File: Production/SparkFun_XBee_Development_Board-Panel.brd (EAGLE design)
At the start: 105.7 x 224.8 mm, 822 parts, among them J1 USB Female Type C Connector, J13 QWIIC_RIGHT_ANGLE, J14 USB Female Type C Connector, J17 USB Female Type C Connector, J23 QWIIC_RIGHT_ANGLE, J24 USB Female Type C Connector, J27 USB Female Type C Connector, J3 USB Female Type C Connector, J33 QWIIC_RIGHT_ANGLE, J34 USB Female Type C Connector, J37 USB Female Type C Connector, J4 QWIIC_RIGHT_ANGLE, J43 QWIIC_RIGHT_ANGLE, J44 USB Female Type C Connector, J47 USB Female Type C Connector, J53 QWIIC_RIGHT_ANGLE, J54 USB Female Type C Connector, J57 USB Female Type C Connector, Q1 3.1A/30V/105mΩ, Q2 3.1A/30V/105mΩ, Q3 3.1A/30V/105mΩ, Q4 3.1A/30V/105mΩ, Q5 3.1A/30V/105mΩ, Q6 3.1A/30V/105mΩ, U1 FSUSB30MUX_MSOP10, U10 FT231XS, U11 FSUSB30MUX_MSOP10, U12 AP63203, U13 ESD Diode, U14 ESD Diode, U15 FT231XS, U16 FSUSB30MUX_MSOP10, U17 AP63203, U18 ESD Diode, U19 ESD Diode, U2 AP63203, U20 FT231XS, U21 FSUSB30MUX_MSOP10, U22 AP63203, U23 ESD Diode, U24 ESD Diode, U25 FT231XS, U26 FSUSB30MUX_MSOP10, U27 AP63203, U28 ESD Diode, U29 ESD Diode, U3 ESD Diode, U30 FT231XS, U4 FSUSB30MUX_MSOP10, U5 ESD Diode, U6 AP63203, U7 FT231XS, U8 ESD Diode, U9 ESD Diode

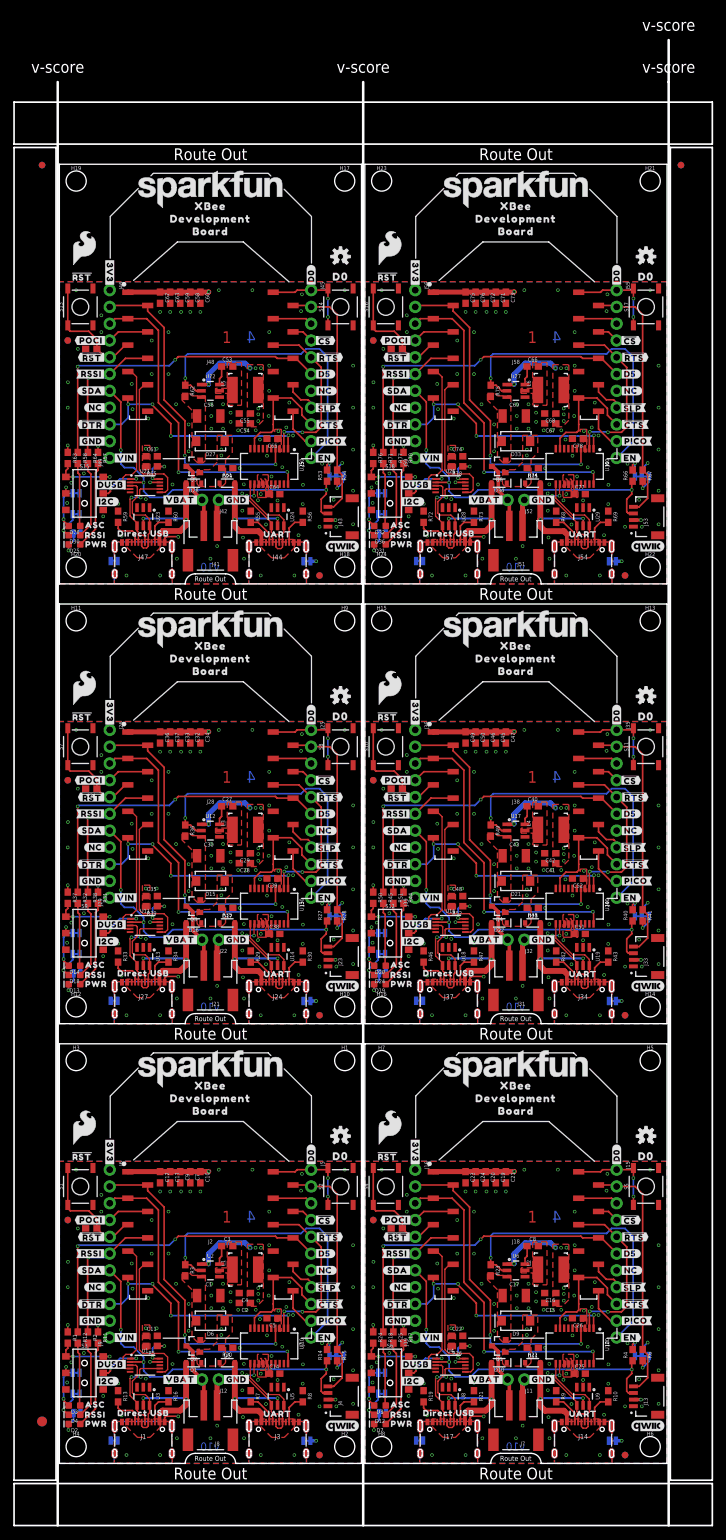
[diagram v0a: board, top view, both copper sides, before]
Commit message: Panelizes new board design
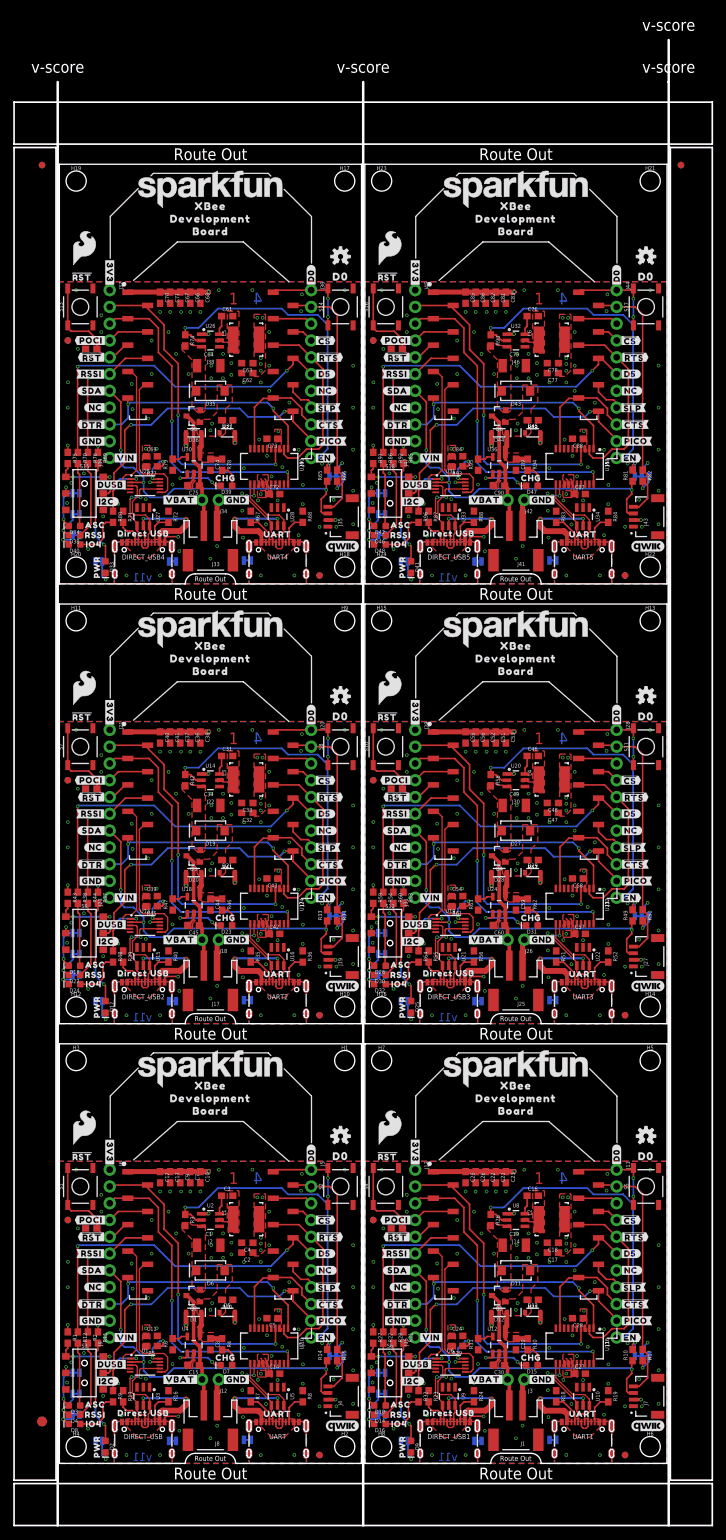
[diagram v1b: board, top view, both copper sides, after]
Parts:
- removed J49, J50, J59, J60: (no value), SparkFun-Connectors:1X01_NO_SILK_STAND
- removed J51: (no value), SparkFun-Connectors:JST-2-SMD
- removed J52: (no value), SparkFun-Connectors:1X02_NO_SILK
- removed J53: QWIIC_RIGHT_ANGLE, SparkFun-Connectors:JST04_1MM_RA
- removed J55, J56: (no value), SparkFun-Connectors:1X10_NO_SILK
- removed J58: (no value), xbee_smart_modem:XBEE3-SMD
- added C79: 10uF, SparkFun-Capacitors:1210
- added C80, C81: 10nF, SparkFun-Capacitors:0603
- added C82, C84, C87, C88: 0.1uF, SparkFun-Capacitors:0603
- added C83: 10uF, SparkFun-Capacitors:0603
- added C85: 10pF, SparkFun-Capacitors:0603
- added C86: 47pF, SparkFun-Capacitors:0603
- added C89, C90: 4.7uF, SparkFun-Capacitors:0603
- added D37, D44, D45: 3A/10V/280mV, SparkFun-DiscreteSemi:SOD-323
- added D38, D39, D46, D47: Yellow, SparkFun-LED:LED-0603
- added D40, D48: GREEN, SparkFun-LED:LED-0603
- added D41: RED, SparkFun-LED:LED-0603
- added D42: BLUE, SparkFun-LED:LED-0603
- added D43: 3A/40V/500mV, SparkFun-DiscreteSemi:SMA-DIODE
- added DIRECT_USB, DIRECT_USB1, DIRECT_USB2, DIRECT_USB3, DIRECT_USB4, UART, UART1, UART2, UART3, UART4: USB Female Type C Connector, SparkFun-Connectors:USB-C-16P-4LAYER-ISOLATED
- added IOLED, IOLED1, IOLED2, IOLED3, IOLED4, IOLED5: JUMPER-SMT_2_NC_TRACE_SILK, SparkFun-Jumpers:SMT-JUMPER_2_NC_TRACE_SILK
- added R79, R95: 2.0k, SparkFun-Resistors:0603
- added R80, R96: 330, SparkFun-Resistors:0603
- added R81, R82, R86, R92: 2.2k, SparkFun-Resistors:0603
- added R83, R84, R87, R88: 5.1k, SparkFun-Resistors:0603
- added R85, R94: 4.7k, SparkFun-Resistors:0603
- added R89, R90: 10k, SparkFun-Resistors:0603
- added R91: 100k, SparkFun-Resistors:0603
- added R93: 100, SparkFun-Resistors:0603
- added U$403: (no value), topmirror:#NC#1
- added U$404: (no value), topmirror:DIRECT_USB33
- added U$405, U$407: (no value), topmirror:DEVELOPMENT1345
- added U$406, U$408: (no value), topmirror:BOARD1346
- added U$409: (no value), botmirror:#DUSB#31
- added U$410, U$411: (no value), top:XBEE339
- added U$412: (no value), top:#D1#AD1#SCL#8
- added U$413: (no value), top:#D8##DTR##27
- added U$414: (no value), top:ASC32
- added U$415: (no value), top:#D2#AD2#SCLK#19
- added U$416: (no value), pot:CHG47
- added U$417: (no value), pot:IO46
- added U$418: (no value), top:#SHLD#740
- added U$419: (no value), top:#SHLD1#741
- added U$420: (no value), top:#IOLED#23
- added U31: FSUSB30MUX_MSOP10, SparkFun-IC-Special-Function:MSOP10
- added U32: AP63203, SparkFun-IC-Power:SOT23-6
- added U33, U34: ESD Diode, SparkFun-DiscreteSemi:SOT-23-6
- added U35: FT231XS, SparkFun-IC-Comms:SSOP20_L
- added U36: MCP73831, SparkFun-IC-Power:SOT23-5
- C15, C29: value 22uF -> 4.7uF
- C16, C28, C42, C54, C67: value 22uF -> 0.1uF
- C17: value 10uF -> 22uF; device SparkFun-Capacitors:1210 -> SparkFun-Capacitors:0603
- C18, C32: value 10nF -> 22uF
- C19: value 10nF -> 10uF; device SparkFun-Capacitors:0603 -> SparkFun-Capacitors:1210
- C20, C35, C51, C65, C66: value 0.1uF -> 10nF
- C21: value 10uF -> 10nF
- C23: value 10pF -> 10uF
- C24, C37, C76: value 47pF -> 0.1uF
- C25, C40: value 0.1uF -> 10pF
- C26: value 0.1uF -> 47pF
- C30: value 10uF -> 4.7uF; device SparkFun-Capacitors:1210 -> SparkFun-Capacitors:0603
- C31, C57, C58: value 10nF -> 0.1uF
- C33, C48, C77, C78: value 0.1uF -> 22uF
- C34: device SparkFun-Capacitors:0603 -> SparkFun-Capacitors:1210
- C36: value 10pF -> 10nF
- C38, C53: value 0.1uF -> 10uF
- C41: value 22uF -> 47pF
- C43, C69: value 10uF -> 0.1uF; device SparkFun-Capacitors:1210 -> SparkFun-Capacitors:0603
- C44, C45: value 10nF -> 4.7uF
- C47: value 10uF -> 22uF
- C49: value 10pF -> 10uF; device SparkFun-Capacitors:0603 -> SparkFun-Capacitors:1210
- C50: value 47pF -> 10nF
- C55: value 22uF -> 10pF
- C56: value 10uF -> 47pF; device SparkFun-Capacitors:1210 -> SparkFun-Capacitors:0603
- C59, C74, C8: value 0.1uF -> 4.7uF
- C60: value 10uF -> 4.7uF
- C62: value 10pF -> 22uF
- C63: value 47pF -> 22uF
- C64: value 0.1uF -> 10uF; device SparkFun-Capacitors:0603 -> SparkFun-Capacitors:1210
- C68: value 22uF -> 10uF
- C70: value 10nF -> 10pF
- C71: value 10nF -> 47pF
- C73: value 10uF -> 0.1uF
- C75: value 10pF -> 4.7uF
- D10, D34: value 3A/10V/280mV -> BLUE; device SparkFun-DiscreteSemi:SOD-323 -> SparkFun-LED:LED-0603
- D11, D35: value 3A/10V/280mV -> 3A/40V/500mV; device SparkFun-DiscreteSemi:SOD-323 -> SparkFun-DiscreteSemi:SMA-DIODE
- D12, D36: value Yellow -> 3A/10V/280mV; device SparkFun-LED:LED-0603 -> SparkFun-DiscreteSemi:SOD-323
- D13: value RED -> 3A/10V/280mV; device SparkFun-LED:LED-0603 -> SparkFun-DiscreteSemi:SOD-323
- D14: value BLUE -> Yellow
- D15: value 3A/40V/500mV -> Yellow; device SparkFun-DiscreteSemi:SMA-DIODE -> SparkFun-LED:LED-0603
- D16: value 3A/10V/280mV -> GREEN; device SparkFun-DiscreteSemi:SOD-323 -> SparkFun-LED:LED-0603
- D17: value 3A/10V/280mV -> RED; device SparkFun-DiscreteSemi:SOD-323 -> SparkFun-LED:LED-0603
- D18: value Yellow -> BLUE
- D19: value RED -> 3A/40V/500mV; device SparkFun-LED:LED-0603 -> SparkFun-DiscreteSemi:SMA-DIODE
- D20: value BLUE -> 3A/10V/280mV; device SparkFun-LED:LED-0603 -> SparkFun-DiscreteSemi:SOD-323
- D21: value 3A/40V/500mV -> 3A/10V/280mV; device SparkFun-DiscreteSemi:SMA-DIODE -> SparkFun-DiscreteSemi:SOD-323
- D22, D23: value 3A/10V/280mV -> Yellow; device SparkFun-DiscreteSemi:SOD-323 -> SparkFun-LED:LED-0603
- D24: value Yellow -> GREEN
- D31, D7: value RED -> Yellow
- D32, D8: value BLUE -> GREEN
- D33, D9: value 3A/40V/500mV -> RED; device SparkFun-DiscreteSemi:SMA-DIODE -> SparkFun-LED:LED-0603
- J1, J17: value USB Female Type C Connector -> (none); device SparkFun-Connectors:USB-C-16P-4LAYER-ISOLATED -> SparkFun-Connectors:JST-2-SMD
- J11: device SparkFun-Connectors:1X02_NO_SILK -> SparkFun-Connectors:1X10_NO_SILK
- J13: value QWIIC_RIGHT_ANGLE -> (none); device SparkFun-Connectors:JST04_1MM_RA -> SparkFun-Connectors:1X10_NO_SILK
- J14: value USB Female Type C Connector -> (none); device SparkFun-Connectors:USB-C-16P-4LAYER-ISOLATED -> xbee_smart_modem:XBEE3-SMD
- J15, J16: device SparkFun-Connectors:1X10_NO_SILK -> SparkFun-Connectors:1X01_NO_SILK_STAND
- J18: device xbee_smart_modem:XBEE3-SMD -> SparkFun-Connectors:1X02_NO_SILK
- J19: value (none) -> QWIIC_RIGHT_ANGLE; device SparkFun-Connectors:1X01_NO_SILK_STAND -> SparkFun-Connectors:JST04_1MM_RA
- J20, J29: device SparkFun-Connectors:1X01_NO_SILK_STAND -> SparkFun-Connectors:1X10_NO_SILK
- J21: device SparkFun-Connectors:JST-2-SMD -> SparkFun-Connectors:1X10_NO_SILK
- J22: device SparkFun-Connectors:1X02_NO_SILK -> xbee_smart_modem:XBEE3-SMD
- J23: value QWIIC_RIGHT_ANGLE -> (none); device SparkFun-Connectors:JST04_1MM_RA -> SparkFun-Connectors:1X01_NO_SILK_STAND
- J24, J47: value USB Female Type C Connector -> (none); device SparkFun-Connectors:USB-C-16P-4LAYER-ISOLATED -> SparkFun-Connectors:1X01_NO_SILK_STAND
- J25: device SparkFun-Connectors:1X10_NO_SILK -> SparkFun-Connectors:JST-2-SMD
- J26: device SparkFun-Connectors:1X10_NO_SILK -> SparkFun-Connectors:1X02_NO_SILK
- J27: value USB Female Type C Connector -> QWIIC_RIGHT_ANGLE; device SparkFun-Connectors:USB-C-16P-4LAYER-ISOLATED -> SparkFun-Connectors:JST04_1MM_RA
- J28: device xbee_smart_modem:XBEE3-SMD -> SparkFun-Connectors:1X10_NO_SILK
- J3, J34: value USB Female Type C Connector -> (none); device SparkFun-Connectors:USB-C-16P-4LAYER-ISOLATED -> SparkFun-Connectors:1X02_NO_SILK
- J30: device SparkFun-Connectors:1X01_NO_SILK_STAND -> xbee_smart_modem:XBEE3-SMD
- J31: device SparkFun-Connectors:JST-2-SMD -> SparkFun-Connectors:1X01_NO_SILK_STAND
- J32: device SparkFun-Connectors:1X02_NO_SILK -> SparkFun-Connectors:1X01_NO_SILK_STAND
- J33: value QWIIC_RIGHT_ANGLE -> (none); device SparkFun-Connectors:JST04_1MM_RA -> SparkFun-Connectors:JST-2-SMD
- J35: value (none) -> QWIIC_RIGHT_ANGLE; device SparkFun-Connectors:1X10_NO_SILK -> SparkFun-Connectors:JST04_1MM_RA
- J37, J44: value USB Female Type C Connector -> (none); device SparkFun-Connectors:USB-C-16P-4LAYER-ISOLATED -> SparkFun-Connectors:1X10_NO_SILK
- J46: device SparkFun-Connectors:1X10_NO_SILK -> xbee_smart_modem:XBEE3-SMD
- J48: device xbee_smart_modem:XBEE3-SMD -> SparkFun-Connectors:1X01_NO_SILK_STAND
- J7: value (none) -> QWIIC_RIGHT_ANGLE; device SparkFun-Connectors:JST-2-SMD -> SparkFun-Connectors:JST04_1MM_RA
- R10, R33, R34, R60: value 5.1k -> 2.2k
- R11: value 1k -> 4.7k
- R17, R44, R70: value 1k -> 2.2k
- R18, R40, R51, R67, R71: value 2.2k -> 5.1k
- R21, R30, R46, R69: value 5.1k -> 4.7k
- R22, R49: value 10k -> 2.2k
- R23, R35, R36: value 10k -> 5.1k
- R24: value 100k -> 5.1k
- R25, R41, R58: value 2.2k -> 10k
- R26: value 100 -> 10k
- R27: value 2.2k -> 100k
- R29: value 5.1k -> 100
- R31: value 1k -> 2.0k
- R32, R64: value 2.2k -> 330
- R37: value 100k -> 4.7k
- R39, R52: value 100 -> 5.1k
- R4, R53: value 2.2k -> 4.7k
- R42, R73: value 5.1k -> 10k
- R43, R59: value 5.1k -> 100k
- R45, R77: value 2.2k -> 100
- R47: value 5.1k -> 2.0k
- R48: value 10k -> 330
- R50, R76: value 100k -> 2.2k
- R57: value 1k -> 10k
- R6: value 2.2k -> 2.0k
- R61: value 10k -> 100
- R62: value 10k -> 4.7k
- R63: value 100k -> 2.0k
- R65: value 100 -> 2.2k
- R75: value 10k -> 100k
- R78: value 100 -> 4.7k
- R9: value 5.1k -> 330
- U$100: device top:#D9##SLP##27 -> top:#D7##CTS##25
- U$101: device top:#TXO#D13#13 -> top:#D9##SLP##27
- U$102: device top:#RXI#D14#15 -> top:#TXO#D13#13
- U$103: device top:##RST##15 -> top:#RXI#D14#15
- U$104: device top:#RSSI#D10#17 -> top:##RST##15
- U$105: device top:#SDA#D11#8 -> top:#RSSI#D10#17
- U$106: device top:#VBAT#5 -> top:#SDA#D11#8
- U$107: device top:#GND#0 -> top:#VBAT#5
- U$108: device top:UART32 -> top:#GND#0
- U$109: device top:#RST#30 -> top:UART32
- U$110: device SparkFun-Aesthetics:SFE_LOGO_NAME_.2 -> top:#RST#30
- U$111: device SparkFun-Aesthetics:SFE_LOGO_FLAME_.2 -> SparkFun-Aesthetics:SFE_LOGO_NAME_.2
- U$112: device top:RSSI31 -> SparkFun-Aesthetics:SFE_LOGO_FLAME_.2
- U$113: device top:#RLED#22 -> top:RSSI31
- U$114: device top:#POCI#D12#24 -> top:#RLED#22
- U$115: device top:#POCI#23 -> top:#POCI#D12#24
- U$116: device top:##DTR##27 -> top:#POCI#23
- U$117: device topmirror:#EN#17 -> top:##DTR##27
- U$119, U$189: device topmirror:#NC#1 -> topmirror:#EN#17
- U$120: device botmirror:#NC#3 -> topmirror:#NC#1
- U$122: device topmirror:#NC#1 -> botmirror:#NC#3
- U$123, U$190: device topmirror:DIRECT_USB33 -> topmirror:#NC#1
- U$124: device topmirror:DEVELOPMENT1345 -> topmirror:DIRECT_USB33
- U$125, U$127: device topmirror:BOARD1346 -> topmirror:DEVELOPMENT1345
- U$126: device topmirror:DEVELOPMENT1345 -> topmirror:BOARD1346
- U$128: device botmirror:#DUSB#31 -> topmirror:BOARD1346
- U$129: device top:XBEE339 -> botmirror:#DUSB#31
- U$131: device top:#D1#AD1#SCL#8 -> top:XBEE339
- U$132: device top:#D8##DTR##27 -> top:#D1#AD1#SCL#8
- U$133: device top:ASC32 -> top:#D8##DTR##27
- U$134: device top:#D2#AD2#SCLK#19 -> top:ASC32
- U$135: device top:##CS##19 -> top:#D2#AD2#SCLK#19
- U$136: device top:##CTS##25 -> pot:CHG47
- U$137: device top:##RTS##24 -> pot:IO46
- U$138: device top:#3V3#1 -> top:#SHLD#740
- U$139: device top:#D0#18 -> top:#SHLD1#741
- U$140: device top:#GND#0 -> top:#IOLED#23
- U$141: device top:#I2C#33 -> top:##CS##19
- U$142: device top:#PICO#23 -> top:##CTS##25
- U$143: device top:#RSSI#16 -> top:##RTS##24
- U$144: device top:#SDA#7 -> top:#3V3#1
- U$145: device top:#SHLD#30 -> top:#D0#18
- U$146: device top:#SHLD1#31 -> top:#GND#0
- U$147: device top:#GND#0 -> top:#I2C#33
- U$148: device bot:#D5#3 -> top:#PICO#23
- U$149: device top:#VIN#4 -> top:#RSSI#16
- U$150: device top:PWR26 -> top:#SDA#7
- U$151: device top:#3V3#1 -> top:#GND#0
- U$152: device top:#GND#0 -> bot:#D5#3
- U$154: device top:##SLP##27 -> top:PWR26
- U$155: device bot:#I2C#31 -> top:#3V3#1
- U$156: device bot:D03 -> top:#GND#0
- U$157: device top:##RST##15 -> top:#VIN#4
- U$158: device top:#VBAT#5 -> top:##SLP##27
- U$159: device top:#ALED#21 -> bot:#I2C#31
- U$160: device top:#PLED#20 -> bot:D03
- U$161: device top:#D0#AD0#18 -> top:##RST##15
- U$162: device top:#D3#AD3#22 -> top:#VBAT#5
- U$163: device top:#D4#PICO#24 -> top:#ALED#21
- U$164: device top:#D5#ASSOC#24 -> top:#PLED#20
- U$165: device top:#D6##RTS##24 -> top:#D0#AD0#18
- U$166: device top:#D7##CTS##25 -> top:#D3#AD3#22
- U$167: device top:#D9##SLP##27 -> top:#D4#PICO#24
- U$168: device top:#TXO#D13#13 -> top:#D5#ASSOC#24
- U$169: device top:#RXI#D14#15 -> top:#D6##RTS##24
- U$170: device top:##RST##15 -> top:#D7##CTS##25
- U$171: device top:#RSSI#D10#17 -> top:#D9##SLP##27
- U$172: device top:#SDA#D11#8 -> top:#TXO#D13#13
- U$173: device top:#VBAT#5 -> top:#RXI#D14#15
- U$174: device top:#GND#0 -> top:##RST##15
- U$175: device top:UART32 -> top:#RSSI#D10#17
- U$176: device top:#RST#30 -> top:#SDA#D11#8
- U$177: device SparkFun-Aesthetics:SFE_LOGO_NAME_.2 -> top:#VBAT#5
- U$178: device SparkFun-Aesthetics:SFE_LOGO_FLAME_.2 -> top:#GND#0
- U$179: device top:RSSI31 -> top:UART32
- U$180: device top:#RLED#22 -> top:#RST#30
- U$181: device top:#POCI#D12#24 -> SparkFun-Aesthetics:SFE_LOGO_NAME_.2
- U$182: device top:#POCI#23 -> SparkFun-Aesthetics:SFE_LOGO_FLAME_.2
- U$183: device top:##DTR##27 -> top:RSSI31
- U$184: device topmirror:#EN#17 -> top:#RLED#22
- U$185: device topmirror:#EN#17 -> top:#POCI#D12#24
- U$186, U$256: device topmirror:#NC#1 -> top:#POCI#23
- U$187: device botmirror:#NC#3 -> top:##DTR##27
- U$188: device botmirror:#NC#3 -> topmirror:#EN#17
- U$19: device top:##CS##19 -> pot:CHG47
- U$191: device topmirror:DEVELOPMENT1345 -> botmirror:#NC#3
- U$192, U$261: device topmirror:BOARD1346 -> botmirror:#NC#3
- U$193, U$260: device topmirror:DEVELOPMENT1345 -> topmirror:#NC#1
- U$194: device topmirror:BOARD1346 -> topmirror:DIRECT_USB33
- U$195: device botmirror:#DUSB#31 -> topmirror:DEVELOPMENT1345
- U$196: device top:XBEE339 -> topmirror:BOARD1346
- U$197: device top:XBEE339 -> topmirror:DEVELOPMENT1345
- U$198: device top:#D1#AD1#SCL#8 -> topmirror:BOARD1346
- U$199: device top:#D8##DTR##27 -> botmirror:#DUSB#31
- U$200: device top:ASC32 -> top:XBEE339
- U$201: device top:#D2#AD2#SCLK#19 -> top:XBEE339
- U$202: device top:##CS##19 -> top:#D1#AD1#SCL#8
- U$203: device top:##CTS##25 -> top:#D8##DTR##27
- U$204: device top:##RTS##24 -> top:ASC32
- U$205: device top:#3V3#1 -> top:#D2#AD2#SCLK#19
- U$206: device top:#D0#18 -> pot:CHG47
- U$207: device top:#GND#0 -> pot:IO46
- U$208: device top:#I2C#33 -> top:#SHLD#740
- U$209: device top:#PICO#23 -> top:#SHLD1#741
- U$210: device top:#RSSI#16 -> top:#IOLED#23
- U$211: device top:#SDA#7 -> top:##CS##19
- U$212: device top:#SHLD#30 -> top:##CTS##25
- U$213: device top:#SHLD1#31 -> top:##RTS##24
- U$214, U$85: device top:#GND#0 -> top:#3V3#1
- U$215: device bot:#D5#3 -> top:#D0#18
- U$216, U$86: device top:#VIN#4 -> top:#GND#0
- U$217: device top:PWR26 -> top:#I2C#33
- U$218: device top:#3V3#1 -> top:#PICO#23
- U$219: device top:#GND#0 -> top:#RSSI#16
- U$220: device top:#VIN#4 -> top:#SDA#7
- U$221: device top:##SLP##27 -> top:#GND#0
- U$222: device bot:#I2C#31 -> bot:#D5#3
- U$223: device bot:D03 -> top:#VIN#4
- U$224: device top:##RST##15 -> top:PWR26
- U$225: device top:#VBAT#5 -> top:#3V3#1
- U$226: device top:#ALED#21 -> top:#GND#0
- U$227: device top:#PLED#20 -> top:#VIN#4
- U$228: device top:#D0#AD0#18 -> top:##SLP##27
- U$229: device top:#D3#AD3#22 -> bot:#I2C#31
- U$230: device top:#D4#PICO#24 -> bot:D03
- U$231: device top:#D5#ASSOC#24 -> top:##RST##15
- U$232: device top:#D6##RTS##24 -> top:#VBAT#5
- U$233: device top:#D7##CTS##25 -> top:#ALED#21
- U$234: device top:#D9##SLP##27 -> top:#PLED#20
- U$235: device top:#TXO#D13#13 -> top:#D0#AD0#18
- U$236: device top:#RXI#D14#15 -> top:#D3#AD3#22
- U$237: device top:##RST##15 -> top:#D4#PICO#24
- U$238: device top:#RSSI#D10#17 -> top:#D5#ASSOC#24
- U$239: device top:#SDA#D11#8 -> top:#D6##RTS##24
- U$240: device top:#VBAT#5 -> top:#D7##CTS##25
- U$241: device top:#GND#0 -> top:#D9##SLP##27
- U$242: device top:UART32 -> top:#TXO#D13#13
- U$243: device top:#RST#30 -> top:#RXI#D14#15
- U$244: device SparkFun-Aesthetics:SFE_LOGO_NAME_.2 -> top:##RST##15
- U$245: device SparkFun-Aesthetics:SFE_LOGO_FLAME_.2 -> top:#RSSI#D10#17
- U$246: device top:RSSI31 -> top:#SDA#D11#8
- U$247: device top:#RLED#22 -> top:#VBAT#5
- U$248: device top:#POCI#D12#24 -> top:#GND#0
- U$249: device top:#POCI#23 -> top:UART32
- U$250: device top:##DTR##27 -> top:#RST#30
- U$251: device topmirror:#EN#17 -> SparkFun-Aesthetics:SFE_LOGO_NAME_.2
- U$252: device topmirror:#EN#17 -> SparkFun-Aesthetics:SFE_LOGO_FLAME_.2
- U$253, U$323: device topmirror:#NC#1 -> top:RSSI31
- U$254: device botmirror:#NC#3 -> top:#RLED#22
- U$255: device botmirror:#NC#3 -> top:#POCI#D12#24
- U$257: device topmirror:DIRECT_USB33 -> top:##DTR##27
- U$258: device topmirror:DEVELOPMENT1345 -> topmirror:#EN#17
- U$259, U$328: device topmirror:BOARD1346 -> topmirror:#EN#17
- U$262: device botmirror:#DUSB#31 -> botmirror:#NC#3
- U$263, U$330: device top:XBEE339 -> topmirror:#NC#1
- U$264: device top:XBEE339 -> topmirror:DIRECT_USB33
- U$265: device top:#D1#AD1#SCL#8 -> topmirror:DEVELOPMENT1345
- U$266: device top:#D8##DTR##27 -> topmirror:BOARD1346
- U$267: device top:ASC32 -> topmirror:DEVELOPMENT1345
- U$268: device top:#D2#AD2#SCLK#19 -> topmirror:BOARD1346
- U$269: device top:##CS##19 -> botmirror:#DUSB#31
- U$270: device top:##CTS##25 -> top:XBEE339
- U$271: device top:##RTS##24 -> top:XBEE339
- U$272: device top:#3V3#1 -> top:#D1#AD1#SCL#8
- U$273: device top:#D0#18 -> top:#D8##DTR##27
- U$274: device top:#GND#0 -> top:ASC32
- U$275: device top:#I2C#33 -> top:#D2#AD2#SCLK#19
- U$276: device top:#PICO#23 -> pot:CHG47
- U$277: device top:#RSSI#16 -> pot:IO46
- U$278: device top:#SDA#7 -> top:#SHLD#740
- U$279: device top:#SHLD#30 -> top:#SHLD1#741
- U$280: device top:#SHLD1#31 -> top:#IOLED#23
- U$281: device top:#GND#0 -> top:##CS##19
- U$282: device bot:#D5#3 -> top:##CTS##25
- U$283: device top:#VIN#4 -> top:##RTS##24
- U$284: device top:PWR26 -> top:#3V3#1
- U$285: device top:#3V3#1 -> top:#D0#18
- U$287: device top:#VIN#4 -> top:#I2C#33
- U$288: device top:##SLP##27 -> top:#PICO#23
- U$289: device bot:#I2C#31 -> top:#RSSI#16
- U$290: device bot:D03 -> top:#SDA#7
- U$291: device top:##RST##15 -> top:#GND#0
- U$292: device top:#VBAT#5 -> bot:#D5#3
- U$293: device top:#ALED#21 -> top:#VIN#4
- U$294: device top:#PLED#20 -> top:PWR26
- U$295: device top:#D0#AD0#18 -> top:#3V3#1
- U$296: device top:#D3#AD3#22 -> top:#GND#0
- U$297: device top:#D4#PICO#24 -> top:#VIN#4
- U$298: device top:#D5#ASSOC#24 -> top:##SLP##27
- U$299: device top:#D6##RTS##24 -> bot:#I2C#31
- U$300: device top:#D7##CTS##25 -> bot:D03
- U$301: device top:#D9##SLP##27 -> top:##RST##15
- U$302: device top:#TXO#D13#13 -> top:#VBAT#5
- U$303: device top:#RXI#D14#15 -> top:#ALED#21
- U$304: device top:##RST##15 -> top:#PLED#20
- U$305: device top:#RSSI#D10#17 -> top:#D0#AD0#18
- U$306: device top:#SDA#D11#8 -> top:#D3#AD3#22
- U$307: device top:#VBAT#5 -> top:#D4#PICO#24
- U$308: device top:#GND#0 -> top:#D5#ASSOC#24
- U$309: device top:UART32 -> top:#D6##RTS##24
- U$310: device top:#RST#30 -> top:#D7##CTS##25
- U$311: device SparkFun-Aesthetics:SFE_LOGO_NAME_.2 -> top:#D9##SLP##27
- U$312: device SparkFun-Aesthetics:SFE_LOGO_FLAME_.2 -> top:#TXO#D13#13
- U$313: device top:RSSI31 -> top:#RXI#D14#15
- U$314: device top:#RLED#22 -> top:##RST##15
- U$315: device top:#POCI#D12#24 -> top:#RSSI#D10#17
- U$316: device top:#POCI#23 -> top:#SDA#D11#8
- U$317: device top:##DTR##27 -> top:#VBAT#5
- U$318: device topmirror:#EN#17 -> top:#GND#0
- U$319: device topmirror:#EN#17 -> top:UART32
- U$320, U$390: device topmirror:#NC#1 -> top:#RST#30
- U$321: device botmirror:#NC#3 -> SparkFun-Aesthetics:SFE_LOGO_NAME_.2
- U$322: device botmirror:#NC#3 -> SparkFun-Aesthetics:SFE_LOGO_FLAME_.2
- U$324: device topmirror:DIRECT_USB33 -> top:#RLED#22
- U$325: device topmirror:DEVELOPMENT1345 -> top:#POCI#D12#24
- U$326: device topmirror:BOARD1346 -> top:#POCI#23
- U$327: device topmirror:DEVELOPMENT1345 -> top:##DTR##27
- U$329: device botmirror:#DUSB#31 -> topmirror:#EN#17
- U$33: device top:##CTS##25 -> pot:IO46
- U$331: device top:XBEE339 -> botmirror:#NC#3
- U$332: device top:#D1#AD1#SCL#8 -> botmirror:#NC#3
- U$333, U$400: device top:#D8##DTR##27 -> topmirror:#NC#1
- U$334: device top:ASC32 -> topmirror:DIRECT_USB33
- U$335: device top:#D2#AD2#SCLK#19 -> topmirror:DEVELOPMENT1345
- U$336: device top:##CS##19 -> topmirror:BOARD1346
- U$337: device top:##CTS##25 -> topmirror:DEVELOPMENT1345
- U$338: device top:##RTS##24 -> topmirror:BOARD1346
- U$339: device top:#3V3#1 -> botmirror:#DUSB#31
- U$340: device top:#D0#18 -> top:XBEE339
- U$341: device top:#GND#0 -> top:XBEE339
- U$342: device top:#I2C#33 -> top:#D1#AD1#SCL#8
- U$343: device top:#PICO#23 -> top:#D8##DTR##27
- U$344: device top:#RSSI#16 -> top:ASC32
- U$345: device top:#SDA#7 -> top:#D2#AD2#SCLK#19
- U$346: device top:#SHLD#30 -> pot:CHG47
- U$347: device top:#SHLD1#31 -> pot:IO46
- U$348: device top:#GND#0 -> top:#SHLD#740
- U$349: device bot:#D5#3 -> top:#SHLD1#741
- U$35: device top:#SHLD#30 -> top:#SHLD#740
- U$350: device top:#VIN#4 -> top:#IOLED#23
- U$351: device top:PWR26 -> top:##CS##19
- U$352: device top:#3V3#1 -> top:##CTS##25
- U$353, U$73: device top:#GND#0 -> top:##RTS##24
- U$354: device top:#VIN#4 -> top:#3V3#1
- U$355: device top:##SLP##27 -> top:#D0#18
- U$356: device bot:#I2C#31 -> top:#GND#0
- U$357: device bot:D03 -> top:#I2C#33
- U$358: device top:##RST##15 -> top:#PICO#23
- U$359: device top:#VBAT#5 -> top:#RSSI#16
- U$36: device top:#SHLD1#31 -> top:#SHLD1#741
- U$360: device top:#ALED#21 -> top:#SDA#7
- U$361: device top:#PLED#20 -> top:#GND#0
- U$362: device top:#D0#AD0#18 -> bot:#D5#3
- U$363: device top:#D3#AD3#22 -> top:#VIN#4
- U$364: device top:#D4#PICO#24 -> top:PWR26
- U$365: device top:#D5#ASSOC#24 -> top:#3V3#1
- U$366: device top:#D6##RTS##24 -> top:#GND#0
- U$367: device top:#D7##CTS##25 -> top:#VIN#4
- U$368: device top:#D9##SLP##27 -> top:##SLP##27
- U$369: device top:#TXO#D13#13 -> bot:#I2C#31
- U$370: device top:#RXI#D14#15 -> bot:D03
- U$372: device top:#RSSI#D10#17 -> top:#VBAT#5
- U$373: device top:#SDA#D11#8 -> top:#ALED#21
- U$374: device top:#VBAT#5 -> top:#PLED#20
- U$375: device top:#GND#0 -> top:#D0#AD0#18
- U$376: device top:UART32 -> top:#D3#AD3#22
- U$377: device top:#RST#30 -> top:#D4#PICO#24
- U$378: device SparkFun-Aesthetics:SFE_LOGO_NAME_.2 -> top:#D5#ASSOC#24
- U$379: device SparkFun-Aesthetics:SFE_LOGO_FLAME_.2 -> top:#D6##RTS##24
- U$380: device top:RSSI31 -> top:#D7##CTS##25
- U$381: device top:#RLED#22 -> top:#D9##SLP##27
- U$382: device top:#POCI#D12#24 -> top:#TXO#D13#13
- U$383: device top:#POCI#23 -> top:#RXI#D14#15
- U$384: device top:##DTR##27 -> top:##RST##15
- U$385: device topmirror:#EN#17 -> top:#RSSI#D10#17
- U$386: device topmirror:#EN#17 -> top:#SDA#D11#8
- U$387: device topmirror:#NC#1 -> top:#VBAT#5
- U$388: device botmirror:#NC#3 -> top:#GND#0
- U$389: device botmirror:#NC#3 -> top:UART32
- U$391: device topmirror:DIRECT_USB33 -> SparkFun-Aesthetics:SFE_LOGO_NAME_.2
- U$392: device topmirror:DEVELOPMENT1345 -> SparkFun-Aesthetics:SFE_LOGO_FLAME_.2
- U$393: device topmirror:BOARD1346 -> top:RSSI31
- U$394: device topmirror:DEVELOPMENT1345 -> top:#RLED#22
- U$395: device topmirror:BOARD1346 -> top:#POCI#D12#24
- U$396: device botmirror:#DUSB#31 -> top:#POCI#23
- U$397: device top:XBEE339 -> top:##DTR##27
- U$398: device top:XBEE339 -> topmirror:#EN#17
- U$399: device top:#D1#AD1#SCL#8 -> topmirror:#EN#17
- U$401: device top:ASC32 -> botmirror:#NC#3
- U$402: device top:#D2#AD2#SCLK#19 -> botmirror:#NC#3
- U$59: device top:##RTS##24 -> top:#IOLED#23
- U$69: device top:#3V3#1 -> top:##CS##19
- U$72: device top:#D0#18 -> top:##CTS##25
- U$74: device top:#I2C#33 -> top:#3V3#1
- U$75: device top:#PICO#23 -> top:#D0#18
- U$76: device top:#RSSI#16 -> top:#GND#0
- U$77: device top:#SDA#7 -> top:#I2C#33
- U$78: device top:#SHLD#30 -> top:#PICO#23
- U$79: device top:#SHLD1#31 -> top:#RSSI#16
- U$80: device top:#GND#0 -> top:#SDA#7
- U$81: device bot:#D5#3 -> top:#GND#0
- U$82: device top:#VIN#4 -> bot:#D5#3
- U$83: device top:PWR26 -> top:#VIN#4
- U$84: device top:#3V3#1 -> top:PWR26
- U$87: device top:##SLP##27 -> top:#VIN#4
- U$88: device bot:#I2C#31 -> top:##SLP##27
- U$89: device bot:D03 -> bot:#I2C#31
- U$90: device top:##RST##15 -> bot:D03
- U$91: device top:#VBAT#5 -> top:##RST##15
- U$92: device top:#ALED#21 -> top:#VBAT#5
- U$93: device top:#PLED#20 -> top:#ALED#21
- U$94: device top:#D0#AD0#18 -> top:#PLED#20
- U$95: device top:#D3#AD3#22 -> top:#D0#AD0#18
- U$96: device top:#D4#PICO#24 -> top:#D3#AD3#22
- U$97: device top:#D5#ASSOC#24 -> top:#D4#PICO#24
- U$98: device top:#D6##RTS##24 -> top:#D5#ASSOC#24
- U$99: device top:#D7##CTS##25 -> top:#D6##RTS##24
- U10, U15: value FT231XS -> ESD Diode; device SparkFun-IC-Comms:SSOP20_L -> SparkFun-DiscreteSemi:SOT-23-6
- U11: value FSUSB30MUX_MSOP10 -> FT231XS; device SparkFun-IC-Special-Function:MSOP10 -> SparkFun-IC-Comms:SSOP20_L
- U12: value AP63203 -> MCP73831; device SparkFun-IC-Power:SOT23-6 -> SparkFun-IC-Power:SOT23-5
- U13, U19: value ESD Diode -> FSUSB30MUX_MSOP10; device SparkFun-DiscreteSemi:SOT-23-6 -> SparkFun-IC-Special-Function:MSOP10
- U14, U8: value ESD Diode -> AP63203; device SparkFun-DiscreteSemi:SOT-23-6 -> SparkFun-IC-Power:SOT23-6
- U16, U21: value FSUSB30MUX_MSOP10 -> ESD Diode; device SparkFun-IC-Special-Function:MSOP10 -> SparkFun-DiscreteSemi:SOT-23-6
- U17: value AP63203 -> FT231XS; device SparkFun-IC-Power:SOT23-6 -> SparkFun-IC-Comms:SSOP20_L
- U18, U24: value ESD Diode -> MCP73831; device SparkFun-DiscreteSemi:SOT-23-6 -> SparkFun-IC-Power:SOT23-5
- U20: value FT231XS -> AP63203; device SparkFun-IC-Comms:SSOP20_L -> SparkFun-IC-Power:SOT23-6
- U22, U27: value AP63203 -> ESD Diode; device SparkFun-IC-Power:SOT23-6 -> SparkFun-DiscreteSemi:SOT-23-6
- U23, U29: value ESD Diode -> FT231XS; device SparkFun-DiscreteSemi:SOT-23-6 -> SparkFun-IC-Comms:SSOP20_L
- U25: value FT231XS -> FSUSB30MUX_MSOP10; device SparkFun-IC-Comms:SSOP20_L -> SparkFun-IC-Special-Function:MSOP10
- U26: value FSUSB30MUX_MSOP10 -> AP63203; device SparkFun-IC-Special-Function:MSOP10 -> SparkFun-IC-Power:SOT23-6
- U30: value FT231XS -> MCP73831; device SparkFun-IC-Comms:SSOP20_L -> SparkFun-IC-Power:SOT23-5
- U4: value FSUSB30MUX_MSOP10 -> MCP73831; device SparkFun-IC-Special-Function:MSOP10 -> SparkFun-IC-Power:SOT23-5
- U6: value AP63203 -> FSUSB30MUX_MSOP10; device SparkFun-IC-Power:SOT23-6 -> SparkFun-IC-Special-Function:MSOP10
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- renumbered J54 to UART5, J57 to DIRECT_USB5
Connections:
- removed net N$40 (its old number): I2C_PU3.3, R40.2
- new net N$100: D47.C, U36.1
- new net N$101: D47.A, R94.2
- new net N$102: D48.A, R96.2
- new net N$38: R35.2, UART2.A5
- new net N$79: C61.2, L5.P$1, U26.5
- new net N$80: D38.A, R76.2
- new net N$81: R77.1, U25.10
- new net N$82: R79.2, U30.5
- new net N$83: D39.C, U30.1
- new net N$84: D39.A, R78.2
- new net N$85: D40.A, R80.2
- new net N$86: I2C_PU5.3, R81.2
- new net N$87: I2C_PU5.1, R82.2
- new net N$88: R84.2, UART5.B5
- new net N$89: R83.2, UART5.A5
- new net N$90: D41.A, R85.2
- new net N$91: D42.A, R86.2
- new net N$92: DIRECT_USB5.B5, R88.2
- new net N$93: DIRECT_USB5.A5, R87.2
- new net N$94: C79.1, D43.C, Q6.2, R90.2, U32.3
- new net N$95: C76.1, U32.6
- new net N$96: C76.2, L6.P$1, U32.5
- new net N$97: D46.A, R92.2
- new net N$98: R93.1, U31.10
- new net N$99: R95.2, U36.5
- new net RLED10: D46.C, RLED5.2
- new net RLED11: D48.C, IOLED5.2
- new net RLED6: D30.C, RLED3.2
- new net RLED7: D32.C, IOLED3.2
- new net RLED8: D38.C, RLED4.2
- new net RLED9: D40.C, IOLED4.2
- net !RESET!1: now also C20.1, J13.5, J14.5; no longer C18.1, J16.5, J18.5
- net !RESET!2: now also C35.1, J21.5, J22.5; no longer C31.1, J26.5, J28.5
- net !RESET!3: now also C50.1, J29.5, J30.5; no longer C44.1, J36.5, J38.5
- net !RESET!4: now also C65.1, J37.5, J38.5; no longer C57.1, J46.5, J48.5
- net !RESET!5: now also C80.1, J45.5, J46.5; no longer C70.1, J56.5, J58.5
- net 3.3V1: now also C17.1, C18.1, C27.1, C28.1, J13.1, J14.1, J7.2, R21.1, R27.1, R29.2, U11.13, U11.14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; no longer C15.1, C16.1, C19.1, C20.1, J13.2, J16.1, J18.1, R17.1, R24.1, R26.2, U10.13, U10.14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
- net 3.3V2: now also C40.1, C41.1, C42.1, C43.1, J19.2, J21.1, J22.1, R43.1, R45.2, U14.1, U17.13, U17.14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; no longer C28.1, C29.1, C34.1, C35.1, J23.2, J26.1, J28.1, R31.1, R39.2, U12.1, U15.13, U15.14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
- net 3.3V3: now also C53.1, C54.1, C55.1, C56.1, C57.1, C58.1, J27.2, J29.1, J30.1, R53.1, R59.1, R61.2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; no longer C41.1, C42.1, C45.1, C46.1, C49.1, C50.1, J33.2, J36.1, J38.1, R44.1, R50.1, R52.2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
- net 3.3V4: now also C66.1, C67.1, C68.1, C69.1, C70.1, C71.1, C72.1, C73.1, J35.2, J37.1, J38.1, R69.1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; no longer C54.1, C55.1, C58.1, C59.1, C60.1, C61.1, C64.1, C65.1, J43.2, J46.1, J48.1, R57.1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
- net 3.3V5: now also C81.1, C82.1, C83.1, C84.1, C85.1, C86.1, C87.1, C88.1, J43.2, J45.1, J46.1, R85.1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; no longer C67.1, C68.1, C71.1, C72.1, C73.1, C74.1, C75.1, C76.1, J53.2, J56.1, J58.1, R70.1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
- net ALED1: now also D10.C; no longer D8.C
- net ALED2: now also D18.C; no longer D14.C
- net ALED3: now also D26.C; no longer D20.C
- net ALED4: now also D34.C; no longer D26.C
- net ALED5: now also D42.C; no longer D32.C
- net D+: now also UART.A6, UART.B6; no longer J3.A6, J3.B6
- net D+1: now also U10.6, U11.11, UART1.A6, UART1.B6; no longer J14.A6, J14.B6, U10.11, U9.6
- net D+2: now also U16.6, U17.11, UART2.A6, UART2.B6; no longer J24.A6, J24.B6, U14.6, U15.11
- net D+3: now also U22.6, U23.11, UART3.A6, UART3.B6; no longer J34.A6, J34.B6, U19.6, U20.11
- net D+4: now also U28.6, U29.11, UART4.A6, UART4.B6; no longer J44.A6, J44.B6, U24.6, U25.11
- net D+5: now also U34.6, U35.11; no longer U29.6, U30.11
- net D-: now also UART.A7, UART.B7; no longer J3.A7, J3.B7
- net D-1: now also U10.4, U11.12, UART1.A7, UART1.B7; no longer J14.A7, J14.B7, U10.12, U9.4
- net D-2: now also U16.4, U17.12, UART2.A7, UART2.B7; no longer J24.A7, J24.B7, U14.4, U15.12
- net D-3: now also U22.4, U23.12, UART3.A7, UART3.B7; no longer J34.A7, J34.B7, U19.4, U20.12
- net D-4: now also U28.4, U29.12, UART4.A7, UART4.B7; no longer J44.A7, J44.B7, U24.4, U25.12
- net D-5: now also U34.4, U35.12; no longer U29.4, U30.12
- net D1: now also J11.1, J14.20; no longer J15.1, J18.20
- net D1/SCL1: now also J11.2, J14.19, J7.4, R17.1; no longer J13.4, J15.2, J18.19, R6.1
- net D1/SCL2: now also J19.4, J20.2, J22.19, R34.1; no longer J23.4, J25.2, J28.19, R28.1
- net D1/SCL3: now also J27.4, J28.2, J30.19, R50.1; no longer J33.4, J35.2, J38.19, R41.1
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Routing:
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- added copper zone on layer 1, net N$26
- added copper zone on layer 1, net N$28
- added copper zone on layer 1, net N$43
- added copper zone on layer 1, net N$45
- added copper zone on layer 1, net N$60
- added copper zone on layer 1, net N$62
- added copper zone on layer 1, net N$77
- added copper zone on layer 1, net N$79
- added copper zone on layer 1, net N$94
- added copper zone on layer 1, net N$96
- removed copper zone on layer 1, net N$22
- removed copper zone on layer 1, net N$24
- removed copper zone on layer 1, net N$35
- removed copper zone on layer 1, net N$37
- removed copper zone on layer 1, net N$48
- removed copper zone on layer 1, net N$50
- removed copper zone on layer 1, net N$61
- removed copper zone on layer 1, net N$63
- removed copper zone on layer 1, net N$74
- removed copper zone on layer 1, net N$76
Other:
- board text added: "v11"
- board text removed: "v10"

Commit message: Updates production panel
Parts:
- moved C21 1.52 mm to (64.5, 43.3)
- moved C22 1.52 mm to (66.0, 43.3)
- moved C36 1.52 mm to (18.3, 109.9)
- moved C37 1.52 mm to (19.8, 109.9)
- moved C51 1.52 mm to (64.5, 109.9)
- moved C52 1.52 mm to (66.0, 109.9)
- moved C66 1.52 mm to (18.3, 176.4)
- moved C67 1.52 mm to (19.8, 176.4)
- moved C7 1.52 mm to (18.3, 43.3)
- moved C81 1.52 mm to (64.5, 176.4)
- moved C82 1.52 mm to (66.0, 176.4)
- moved C9 1.52 mm to (19.8, 43.3)
- moved U$139 0.08 mm to (67.1, 3.38)
- moved U$209 0.08 mm to (20.8, 69.9)
- moved U$279 0.08 mm to (67.1, 69.9)
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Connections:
- net RLED11 renamed IOLED5
- net RLED7 renamed IOLED3
- net RLED9 renamed IOLED4
- removed net RLED10: D46.C, RLED5.2
- removed net RLED6: D30.C, RLED3.2
- removed net RLED8: D38.C, RLED4.2
- new net IOLED: D8.C, IOLED.2
- new net IOLED1: D16.C, IOLED1.2
- new net IOLED2: D24.C, IOLED2.2
- net RLED1: now also D14.C, RLED1.2; no longer D8.C, IOLED.2
- net RLED2: now also D22.C, RLED2.2; no longer D14.C, RLED1.2
- net RLED3: now also D30.C, RLED3.2; no longer D16.C, IOLED1.2
- net RLED4: now also D38.C, RLED4.2; no longer D22.C, RLED2.2
- net RLED5: now also D46.C, RLED5.2; no longer D24.C, IOLED2.2
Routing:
- net RLED8: track 4.14 -> 0.00 mm, vias 1 -> 0
- net RLED10: track 4.14 -> 0.00 mm, vias 1 -> 0
- net RLED6: track 4.14 -> 0.00 mm, vias 1 -> 0
- net IOLED1: track 0.00 -> 3.07 mm, vias 0 -> 1
- net IOLED2: track 0.00 -> 3.07 mm, vias 0 -> 1
- net IOLED: track 0.00 -> 3.07 mm, vias 0 -> 1
- net RLED5: track 3.07 -> 4.14 mm
- net RLED1: track 3.07 -> 4.14 mm
- net RLED3: track 3.07 -> 4.14 mm
- net VIN4: track 25.0 -> 24.4 mm
- net VIN3: track 25.0 -> 24.4 mm
- net VIN5: track 25.0 -> 24.4 mm
- net VIN2: track 25.0 -> 24.4 mm
- net VIN1: track 25.0 -> 24.4 mm
- net VIN: track 25.0 -> 24.4 mm

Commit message: Updates production files
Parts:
- moved C42 8.39 mm to (32.3, 88.5), turned to 180 degrees
- moved C43 8.39 mm to (32.5, 80.1), turned to 0 degrees
- moved C72 8.39 mm to (32.3, 155.1), turned to 180 degrees
- moved C73 8.39 mm to (32.5, 146.7), turned to 0 degrees
- moved C57 8.39 mm to (78.5, 88.5), turned to 180 degrees
- moved C58 8.39 mm to (78.7, 80.1), turned to 0 degrees
- moved C87 8.39 mm to (78.5, 155.1), turned to 180 degrees
- moved C88 8.39 mm to (78.7, 146.7), turned to 0 degrees
- moved C14 8.39 mm to (32.3, 22.0), turned to 180 degrees
- moved C5 8.39 mm to (32.5, 13.6), turned to 0 degrees
- moved C27 8.39 mm to (78.5, 22.0), turned to 180 degrees
- moved C28 8.39 mm to (78.7, 13.6), turned to 0 degrees
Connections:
- new net N$108: C87.1, U35.13, U35.14, U35.3
- new net N$18: C14.1, U7.13, U7.14, U7.3
- new net N$36: C27.1, U11.13, U11.14, U11.3
- new net N$54: C42.1, U17.13, U17.14, U17.3
- new net N$72: C57.1, U23.13, U23.14, U23.3
- new net N$90: C72.1, U29.13, U29.14, U29.3
- net 3.3V: no longer C14.1, C5.1, U7.13, U7.14, U7.15, U7.3
- net 3.3V1: no longer C27.1, C28.1, U11.13, U11.14, U11.15, U11.3
- net 3.3V2: no longer C42.1, C43.1, U17.13, U17.14, U17.15, U17.3
- net 3.3V3: no longer C57.1, C58.1, U23.13, U23.14, U23.15, U23.3
- net 3.3V4: no longer C72.1, C73.1, U29.13, U29.14, U29.15, U29.3
- net 3.3V5: no longer C87.1, C88.1, U35.13, U35.14, U35.15, U35.3
- net V_USB: now also C5.1, U7.15
- net V_USB1: now also C28.1, U11.15
- net V_USB2: now also C43.1, U17.15
- net V_USB3: now also C58.1, U23.15
- net V_USB4: now also C73.1, U29.15
- net V_USB5: now also C88.1, U35.15
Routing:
- net N$36: track 0.00 -> 11.5 mm
- net N$72: track 0.00 -> 11.5 mm
- net N$18: track 0.00 -> 11.5 mm
- net N$108: track 0.00 -> 11.5 mm
- net N$90: track 0.00 -> 11.5 mm
- net N$54: track 0.00 -> 11.5 mm
- net V_USB5: track 27.6 -> 34.0 mm, vias 3 -> 4
- net V_USB4: track 27.6 -> 34.0 mm, vias 3 -> 4
- net V_USB1: track 27.6 -> 34.0 mm, vias 3 -> 4
- net V_USB3: track 27.6 -> 34.0 mm, vias 3 -> 4
- net V_USB: track 27.6 -> 34.0 mm, vias 3 -> 4
- net V_USB2: track 27.6 -> 34.0 mm, vias 3 -> 4
- net 3.3V5: vias 14 -> 13
- net 3.3V4: vias 14 -> 13
- net 3.3V3: vias 14 -> 13
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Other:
- board text added: "v12"
- board text removed: "v11"
